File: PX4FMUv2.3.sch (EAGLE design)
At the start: 252 parts, among them J201 DF13C-6P-1.25V, J202 DF13C-6P-1.25V, J203 DF13C-6P-1.25V, J204 DF13C-6P-1.25V, J301 47346-0001, J302 DF13C-4P-1.25V, J401 DF13C-4P-1.25V, J402 DF13C-3P-1.25V, J403 DF13C-7P-1.25V, J404 DF13C-5P-1.25V, J405 DF13C-4P-1.25V, J601 DF13C-6P-1.25V, J701 DF13C-2P-1.25V, J702 DF13C-3P-1.25V, J801 JST-ZH-3, J901 HEADER-3X163X16RA, M3_MOUNT1101 MOUNT-HOLE3.1MM, M3_MOUNT1102 MOUNT-HOLE3.1MM, M3_MOUNT1103 MOUNT-HOLE3.1MM, M3_MOUNT1104 MOUNT-HOLE3.1MM, U101 STM32F4X7VX, U102 FM25V01, U201 TXS0108QFN20, U202 TXS0108QFN20, U301 2908-05WB-MG, U401 MAX3051, U501 L3GD20, U502 L3GD20H, U503 MS5611-01BA, U701 TCA62724FMG, U702 LT3469, U703 LRTB GFTG-T7AW-1+V7A7-29+R5T9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, U801 STM32F10XCXT6, U901 TXS0108QFN20, U902 TXS0108QFN20, U903 74LVC2G240, X101 3.2x2.5 mm / 24 MHz / 15 ppm, X801 3.2x2.5 mm / 24 MHz / 15 ppm

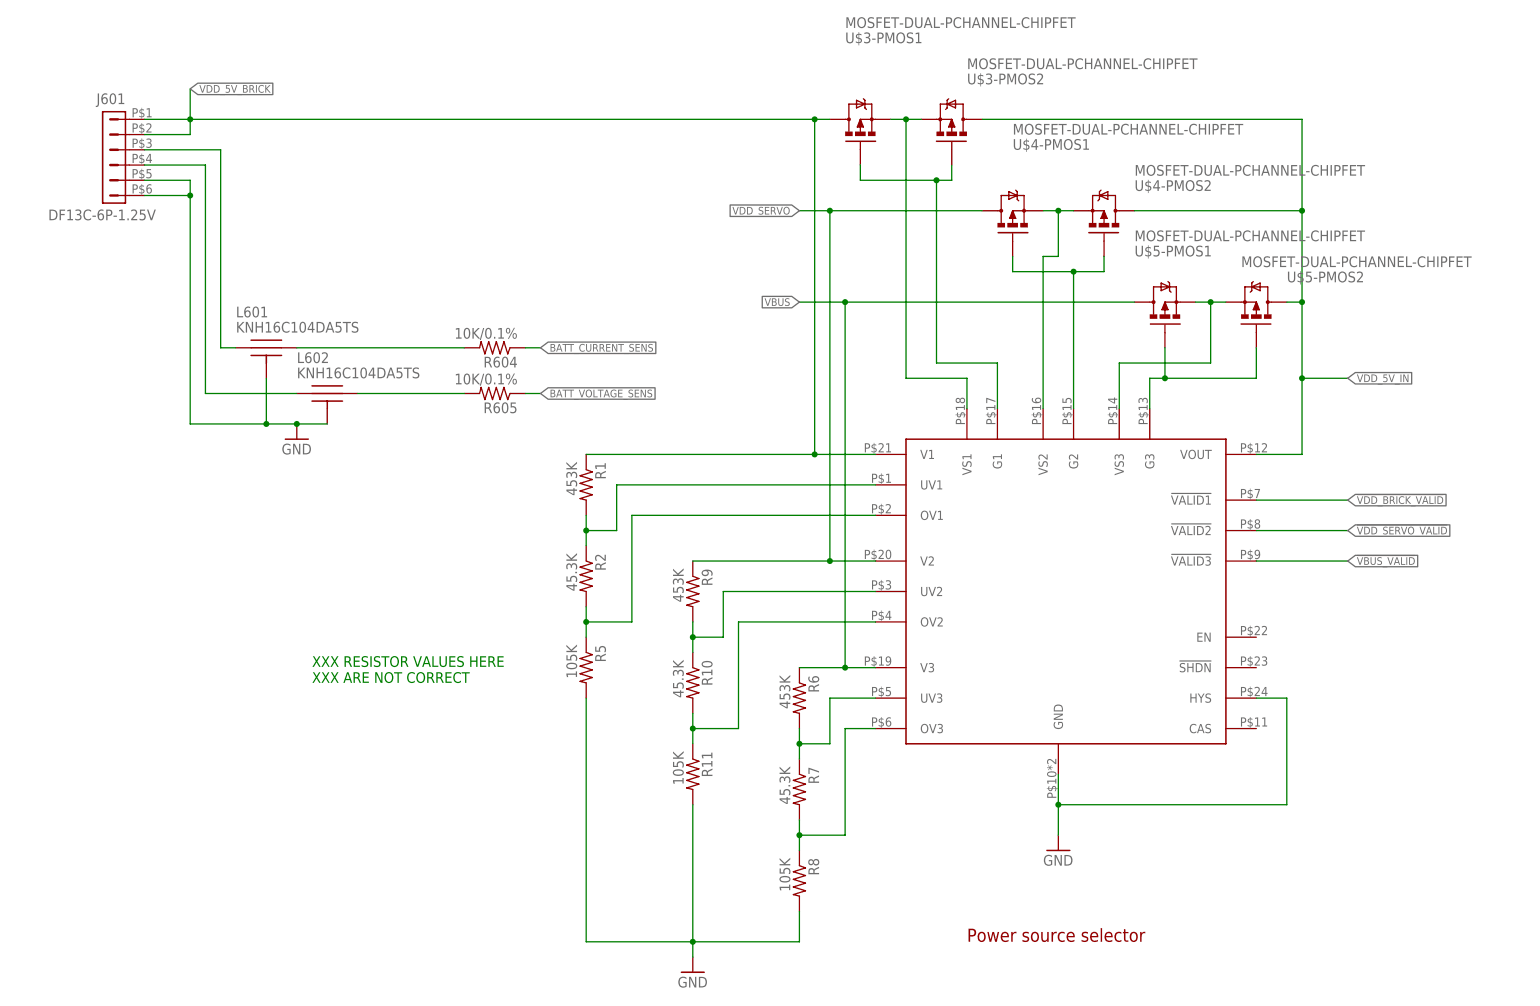
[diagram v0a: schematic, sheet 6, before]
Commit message: Updates to reflect questions asked on mailing list https://groups.google.com/forum/#!topicsearchin/px4users/mosfet%7Csort:date/px4users/fcfwdMKPhbI
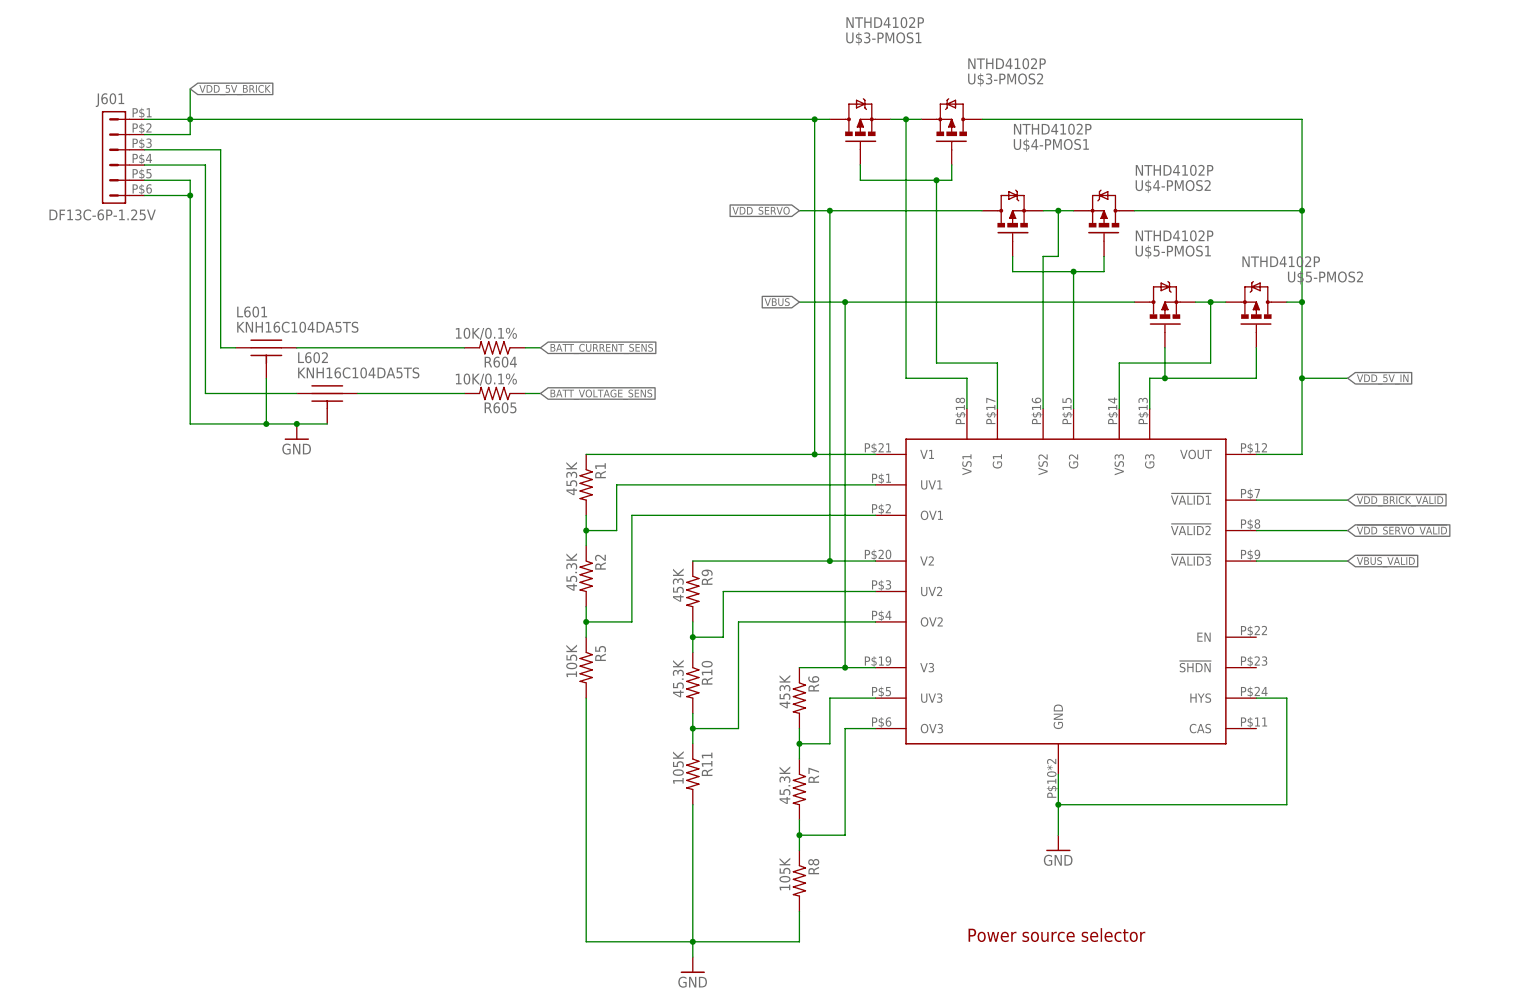
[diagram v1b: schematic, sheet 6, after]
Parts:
- B601: value MS621FE -> DO NOT PLACE
- U$3, U$4, U$5: value MOSFET-DUAL-PCHANNEL-CHIPFET -> NTHD4102P
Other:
- note removed: "PAGE SIGNOFF LM"
- note removed: "XXX CHECK DEN SIGNAL, NOT CLEAR IN CURRENT DATASHEET"
- note removed: "XXX RESISTOR VALUES HERE XXX ARE NOT CORRECT"
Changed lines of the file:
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@@
 <?xml version="1.0" encoding="utf-8"?>
 <!DOCTYPE eagle SYSTEM "eagle.dtd">
-<eagle version="6.5.0">
+<eagle version="6.4">
 <drawing>
 <settings>
@@
 <attribute name="PARTNO" value="DF13C-4P-1.25V(20)"/>
 </part>
-<part name="B601" library="pixhawk2" deviceset="MS621FE" device="">
+<part name="B601" library="pixhawk2" deviceset="MS621FE" device="" value="DO NOT PLACE">
 <attribute name="PARTNO" value="MS621FE-FL11E"/>
 </part>
@@
 <attribute name="PARTNO" value="*"/>
 </part>
-<part name="U$3" library="pixhawk2" deviceset="MOSFET-DUAL-PCHANNEL" device="-CHIPFET">
+<part name="U$3" library="pixhawk2" deviceset="MOSFET-DUAL-PCHANNEL" device="-CHIPFET" value="NTHD4102P">
 <attribute name="PARTNO" value="*"/>
 </part>
-<part name="U$4" library="pixhawk2" deviceset="MOSFET-DUAL-PCHANNEL" device="-CHIPFET">
+<part name="U$4" library="pixhawk2" deviceset="MOSFET-DUAL-PCHANNEL" device="-CHIPFET" value="NTHD4102P">
 <attribute name="PARTNO" value="*"/>
 </part>
-<part name="U$5" library="pixhawk2" deviceset="MOSFET-DUAL-PCHANNEL" device="-CHIPFET">
+<part name="U$5" library="pixhawk2" deviceset="MOSFET-DUAL-PCHANNEL" device="-CHIPFET" value="NTHD4102P">
 <attribute name="PARTNO" value="*"/>
 </part>
@@
 <text x="15.24" y="129.54" size="1.4224" layer="91">NOTE: place 10uF cap
 close to gyros</text>
-<text x="165.1" y="27.94" size="2.54" layer="98">PAGE SIGNOFF LM</text>
-<text x="78.486" y="34.29" size="1.778" layer="91">XXX CHECK DEN SIGNAL,
-NOT CLEAR IN CURRENT DATASHEET</text>
 <wire x1="5.08" y1="162.56" x2="5.08" y2="101.6" width="0.1524" layer="94" style="dashdot"/>
 <wire x1="5.08" y1="101.6" x2="127" y2="101.6" width="0.1524" layer="94" style="dashdot"/>
@@
 <plain>
 <text x="165.1" y="17.78" size="2.1844" layer="94">Power source selector</text>
-<text x="55.88" y="60.96" size="1.778" layer="91">XXX RESISTOR VALUES HERE
-XXX ARE NOT CORRECT</text>
 </plain>
 <instances>
